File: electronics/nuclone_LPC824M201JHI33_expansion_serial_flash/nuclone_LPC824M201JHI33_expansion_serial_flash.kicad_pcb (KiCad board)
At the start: 2 copper layers, 45.8 x 25.5 mm, 23 parts, among them J1 nuclone_small_left, J2 nuclone_small_right, J3 DevBoardUartInput, J4 Conn_02x06_Odd_Even, U1 generic 25XNN serial flash

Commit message: LED place and route done, routing comleted
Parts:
- moved D2 12.7 mm to (75.6, 78.7)
- moved R10 12.7 mm to (73.0, 78.7)
- moved D1 12.7 mm to (75.6, 80.1)
- moved R9 12.7 mm to (73.0, 80.1)
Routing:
- net /VBUS: track 0.00 -> 29.4 mm
- net /LED1: track 0.00 -> 10.9 mm, vias 0 -> 1
- net /LED0: track 0.00 -> 8.07 mm, vias 0 -> 1
- net /VSS: track 2.45 -> 5.60 mm, vias 2 -> 3
- net Net-(D2-Pad2): track 0.00 -> 1.20 mm
- net Net-(D1-Pad2): track 0.00 -> 1.20 mm
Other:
- board text added: "Activity"
- board text added: "Blinky"
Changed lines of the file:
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@@
   (general
     (thickness 1.6)
-    (drawings 80)
-    (tracks 129)
+    (drawings 82)
+    (tracks 160)
     (zones 0)
     (modules 23)
@@
   )
   (module SquantorRcl:R_0402_hand (layer F.Cu)
-    (at 74.1 66 180)
+    (at 73 78.7 180)
     (descr "Resistor SMD 0402, reflow soldering, Vishay (see dcrcw.pdf)")
     (tags "resistor 0402")
@@
   )
   (module SquantorRcl:R_0402_hand (layer F.Cu)
-    (at 74.1 67.4 180)
+    (at 73 80.1 180)
     (descr "Resistor SMD 0402, reflow soldering, Vishay (see dcrcw.pdf)")
     (tags "resistor 0402")
@@
   )
   (module SquantorDiodes:LED_0603_hand (layer F.Cu)
-    (at 76.7 66 180)
+    (at 75.6 78.7 180)
     (descr "LED SMD 0603, reflow soldering, general purpose")
     (tags "LED 0603")
@@
   )
   (module SquantorDiodes:LED_0603_hand (layer F.Cu)
-    (at 76.7 67.4 180)
+    (at 75.6 80.1 180)
     (descr "LED SMD 0603, reflow soldering, general purpose")
     (tags "LED 0603")
@@
     (fp_line (start -0.5 -0.6) (end 0.5 -0.6) (layer B.SilkS) (width 0.15))
   )
+  (gr_text Blinky (at 75.7 77.2) (layer F.SilkS)
+    (effects (font (size 0.8 0.8) (thickness 0.12)))
+  )
+  (gr_text Activity (at 75.5 81.4) (layer F.SilkS)
+    (effects (font (size 0.8 0.8) (thickness 0.12)))
+  )
   (gr_text SIO3 (at 90 77.5) (layer F.SilkS)
     (effects (font (size 0.8 0.8) (thickness 0.12)))
@@
   (gr_line (start 63.1 99.1) (end 107.1 99.1) (layer Edge.Cuts) (width 0.15))
   (gr_line (start 62.2 74.5) (end 62.2 98.2) (layer Edge.Cuts) (width 0.15))
+  (segment (start 77 92.4) (end 77 94.1) (width 1) (layer F.Cu) (net 1))
+  (segment (start 77 94.1) (end 75.9 95.2) (width 1) (layer F.Cu) (net 1))
+  (segment (start 75.9 95.2) (end 69.9 95.2) (width 1) (layer F.Cu) (net 1))
+  (segment (start 69.9 95.2) (end 68.3 93.6) (width 1) (layer F.Cu) (net 1))
+  (segment (start 68.3 93.6) (end 68.3 78.4) (width 1) (layer F.Cu) (net 1))
+  (segment (start 67.37 77.47) (end 66.04 77.47) (width 1) (layer F.Cu) (net 1))
+  (segment (start 68.3 78.4) (end 67.37 77.47) (width 1) (layer F.Cu) (net 1))
   (via (at 87.5 84.1) (size 0.6) (drill 0.3) (layers F.Cu B.Cu) (net 8))
   (segment (start 87.505 84.105) (end 87.5 84.1) (width 0.4) (layer F.Cu) (net 8))
@@
   (via (at 82 84) (size 0.6) (drill 0.3) (layers F.Cu B.Cu) (net 8))
   (segment (start 82 83.2) (end 82 84) (width 0.4) (layer F.Cu) (net 8))
+  (via (at 77.5 79.4) (size 0.6) (drill 0.3) (layers F.Cu B.Cu) (net 8))
+  (segment (start 77.5 79.8) (end 77.5 79.4) (width 0.2) (layer F.Cu) (net 8))
+  (segment (start 77.2 80.1) (end 77.5 79.8) (width 0.2) (layer F.Cu) (net 8))
+  (segment (start 76.45 80.1) (end 77.2 80.1) (width 0.2) (layer F.Cu) (net 8))
+  (segment (start 77.5 79) (end 77.5 79.4) (width 0.2) (layer F.Cu) (net 8))
+  (segment (start 77.2 78.7) (end 77.5 79) (width 0.2) (layer F.Cu) (net 8))
+  (segment (start 76.45 78.7) (end 77.2 78.7) (width 0.2) (layer F.Cu) (net 8))
   (segment (start 63.5 74.93) (end 66.04 74.93) (width 1) (layer B.Cu) (net 9))
   (segment (start 104.14 74.93) (end 106.68 74.93) (width 1) (layer B.Cu) (net 9))
@@
   (segment (start 87.5 77.7) (end 87.5 77.15) (width 0.2) (layer F.Cu) (net 28))
   (segment (start 87.505 77.705) (end 87.5 77.7) (width 0.2) (layer F.Cu) (net 28))
+  (segment (start 74.75 80.1) (end 73.55 80.1) (width 0.2) (layer F.Cu) (net 29))
+  (segment (start 74.75 78.7) (end 73.55 78.7) (width 0.2) (layer F.Cu) (net 30))
+  (segment (start 66.04 82.55) (end 66.95 82.55) (width 0.2) (layer B.Cu) (net 35))
+  (via (at 69.3 82) (size 0.6) (drill 0.3) (layers F.Cu B.Cu) (net 35))
+  (segment (start 67.5 82) (end 69.3 82) (width 0.2) (layer B.Cu) (net 35))
+  (segment (start 66.95 82.55) (end 67.5 82) (width 0.2) (layer B.Cu) (net 35))
+  (segment (start 69.3 82) (end 69.7 82) (width 0.2) (layer F.Cu) (net 35))
+  (segment (start 69.7 82) (end 70 81.7) (width 0.2) (layer F.Cu) (net 35))
+  (segment (start 70 81.7) (end 70 80.6) (width 0.2) (layer F.Cu) (net 35))
+  (segment (start 70.5 80.1) (end 72.45 80.1) (width 0.2) (layer F.Cu) (net 35))
+  (segment (start 70 80.6) (end 70.5 80.1) (width 0.2) (layer F.Cu) (net 35))
+  (segment (start 63.5 82.55) (end 64.85 81.2) (width 0.2) (layer B.Cu) (net 36))
+  (via (at 69.3 81.2) (size 0.6) (drill 0.3) (layers F.Cu B.Cu) (net 36))
+  (segment (start 64.85 81.2) (end 69.3 81.2) (width 0.2) (layer B.Cu) (net 36))
+  (segment (start 69.3 80.6) (end 69.3 81.2) (width 0.2) (layer F.Cu) (net 36))
+  (segment (start 71.2 78.7) (end 69.3 80.6) (width 0.2) (layer F.Cu) (net 36))
+  (segment (start 72.45 78.7) (end 71.2 78.7) (width 0.2) (layer F.Cu) (net 36))
   (segment (start 102.59 80.01) (end 101.3 81.3) (width 0.2) (layer F.Cu) (net 41))
   (segment (start 94.62 81.3) (end 93.36 82.56) (width 0.2) (layer F.Cu) (net 41))

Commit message: fixed DRC error
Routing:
- net /VDD: track 71.0 -> 68.5 mm
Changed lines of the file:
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@@
     (thickness 1.6)
     (drawings 82)
-    (tracks 160)
+    (tracks 159)
     (zones 0)
     (modules 23)
@@
   (segment (start 76.45 78.7) (end 77.2 78.7) (width 0.2) (layer F.Cu) (net 8))
   (segment (start 63.5 74.93) (end 66.04 74.93) (width 1) (layer B.Cu) (net 9))
-  (segment (start 104.14 74.93) (end 106.68 74.93) (width 1) (layer B.Cu) (net 9))
   (segment (start 87.6 88.95) (end 88.45 88.95) (width 0.4) (layer F.Cu) (net 9))
   (segment (start 88.45 88.95) (end 88.9 88.5) (width 0.4) (layer F.Cu) (net 9))

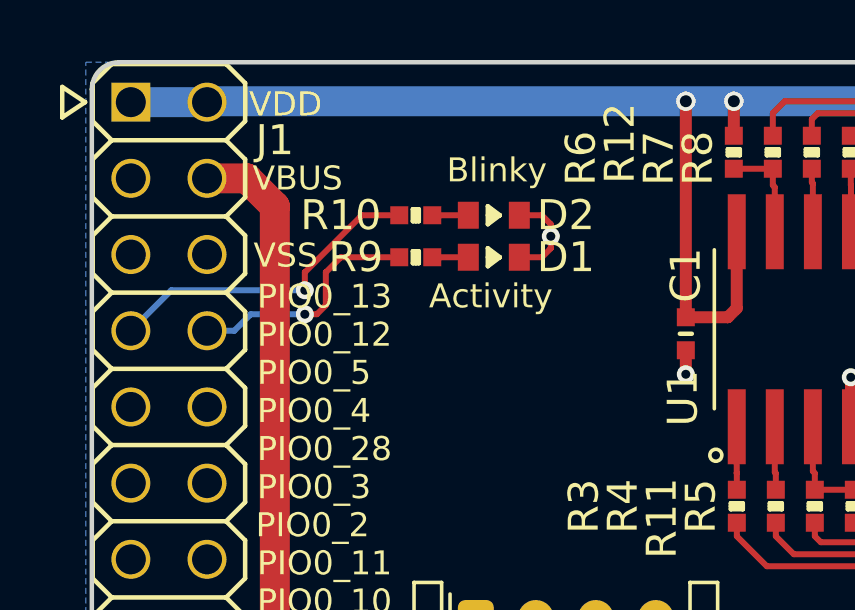
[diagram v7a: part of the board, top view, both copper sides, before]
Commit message: nicer LED placement
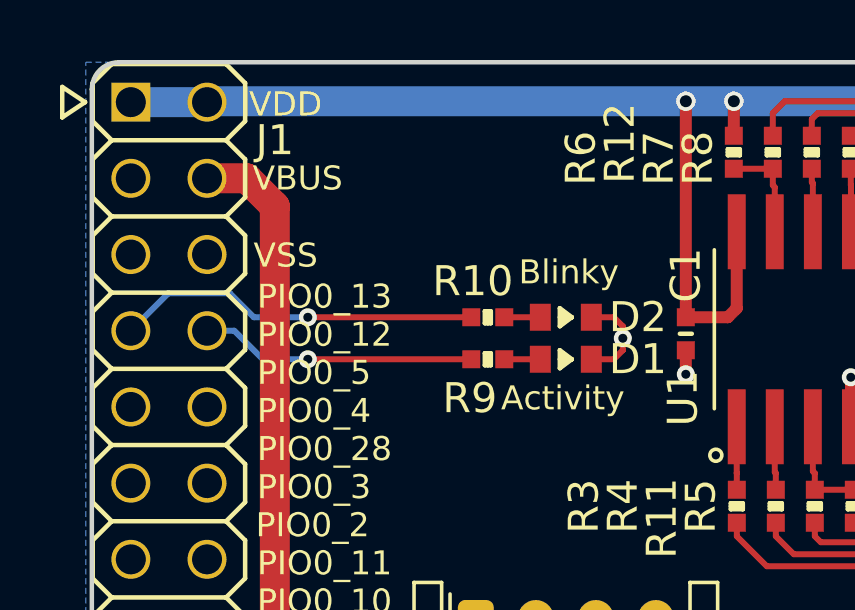
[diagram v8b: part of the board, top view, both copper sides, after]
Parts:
- moved D1 4.16 mm to (78.0, 83.5)
- moved R9 4.16 mm to (75.4, 83.5)
- moved D2 4.16 mm to (78.0, 82.1)
- moved R10 4.16 mm to (75.4, 82.1)
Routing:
- net /LED1: track 10.9 -> 12.2 mm
- net /LED0: track 8.07 -> 9.20 mm
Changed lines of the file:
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@@
     (thickness 1.6)
     (drawings 82)
-    (tracks 159)
+    (tracks 155)
     (zones 0)
     (modules 23)
@@
   )
   (module SquantorRcl:R_0402_hand (layer F.Cu)
-    (at 73 78.7 180)
+    (at 75.4 82.1 180)
     (descr "Resistor SMD 0402, reflow soldering, Vishay (see dcrcw.pdf)")
     (tags "resistor 0402")
     (attr smd)
-    (fp_text reference R10 (at 2.5 0) (layer F.SilkS)
-      (effects (font (size 1 1) (thickness 0.15)))
-    )
-    (fp_text value 4.7K (at 0 1.8) (layer F.Fab)
+    (fp_text reference R10 (at 0.5 1.2) (layer F.SilkS)
+      (effects (font (size 1 1) (thickness 0.15)))
+    )
+    (fp_text value 4.7K (at 0.7 1.2) (layer F.Fab)
       (effects (font (size 1 1) (thickness 0.15)))
     )
@@
   )
   (module SquantorRcl:R_0402_hand (layer F.Cu)
-    (at 73 80.1 180)
+    (at 75.4 83.5 180)
     (descr "Resistor SMD 0402, reflow soldering, Vishay (see dcrcw.pdf)")
     (tags "resistor 0402")
     (attr smd)
-    (fp_text reference R9 (at 2 0) (layer F.SilkS)
-      (effects (font (size 1 1) (thickness 0.15)))
-    )
-    (fp_text value 4.7K (at 0 1.8) (layer F.Fab)
+    (fp_text reference R9 (at 0.6 -1.3) (layer F.SilkS)
+      (effects (font (size 1 1) (thickness 0.15)))
+    )
+    (fp_text value 4.7K (at 0.7 -1.3) (layer F.Fab)
       (effects (font (size 1 1) (thickness 0.15)))
     )
@@
   )
   (module SquantorDiodes:LED_0603_hand (layer F.Cu)
-    (at 75.6 78.7 180)
+    (at 78 82.1 180)
     (descr "LED SMD 0603, reflow soldering, general purpose")
     (tags "LED 0603")
@@
   )
   (module SquantorDiodes:LED_0603_hand (layer F.Cu)
-    (at 75.6 80.1 180)
+    (at 78 83.5 180)
     (descr "LED SMD 0603, reflow soldering, general purpose")
     (tags "LED 0603")
@@
     (fp_line (start -0.5 -0.6) (end 0.5 -0.6) (layer B.SilkS) (width 0.15))
   )
-  (gr_text Blinky (at 75.7 77.2) (layer F.SilkS)
-    (effects (font (size 0.8 0.8) (thickness 0.12)))
-  )
-  (gr_text Activity (at 75.5 81.4) (layer F.SilkS)
+  (gr_text Blinky (at 78.1 80.6) (layer F.SilkS)
+    (effects (font (size 0.8 0.8) (thickness 0.12)))
+  )
+  (gr_text Activity (at 77.9 84.8) (layer F.SilkS)
     (effects (font (size 0.8 0.8) (thickness 0.12)))
   )
@@
   (via (at 82 84) (size 0.6) (drill 0.3) (layers F.Cu B.Cu) (net 8))
   (segment (start 82 83.2) (end 82 84) (width 0.4) (layer F.Cu) (net 8))
-  (via (at 77.5 79.4) (size 0.6) (drill 0.3) (layers F.Cu B.Cu) (net 8))
-  (segment (start 77.5 79.8) (end 77.5 79.4) (width 0.2) (layer F.Cu) (net 8))
-  (segment (start 77.2 80.1) (end 77.5 79.8) (width 0.2) (layer F.Cu) (net 8))
-  (segment (start 76.45 80.1) (end 77.2 80.1) (width 0.2) (layer F.Cu) (net 8))
-  (segment (start 77.5 79) (end 77.5 79.4) (width 0.2) (layer F.Cu) (net 8))
-  (segment (start 77.2 78.7) (end 77.5 79) (width 0.2) (layer F.Cu) (net 8))
-  (segment (start 76.45 78.7) (end 77.2 78.7) (width 0.2) (layer F.Cu) (net 8))
+  (via (at 79.9 82.8) (size 0.6) (drill 0.3) (layers F.Cu B.Cu) (net 8))
+  (segment (start 79.9 83.2) (end 79.9 82.8) (width 0.2) (layer F.Cu) (net 8))
+  (segment (start 79.6 83.5) (end 79.9 83.2) (width 0.2) (layer F.Cu) (net 8))
+  (segment (start 78.85 83.5) (end 79.6 83.5) (width 0.2) (layer F.Cu) (net 8))
+  (segment (start 79.9 82.4) (end 79.9 82.8) (width 0.2) (layer F.Cu) (net 8))
+  (segment (start 79.6 82.1) (end 79.9 82.4) (width 0.2) (layer F.Cu) (net 8))
+  (segment (start 78.85 82.1) (end 79.6 82.1) (width 0.2) (layer F.Cu) (net 8))
   (segment (start 63.5 74.93) (end 66.04 74.93) (width 1) (layer B.Cu) (net 9))
   (segment (start 87.6 88.95) (end 88.45 88.95) (width 0.4) (layer F.Cu) (net 9))
@@
   (segment (start 87.5 77.7) (end 87.5 77.15) (width 0.2) (layer F.Cu) (net 28))
   (segment (start 87.505 77.705) (end 87.5 77.7) (width 0.2) (layer F.Cu) (net 28))
-  (segment (start 74.75 80.1) (end 73.55 80.1) (width 0.2) (layer F.Cu) (net 29))
-  (segment (start 74.75 78.7) (end 73.55 78.7) (width 0.2) (layer F.Cu) (net 30))
-  (segment (start 66.04 82.55) (end 66.95 82.55) (width 0.2) (layer B.Cu) (net 35))
-  (via (at 69.3 82) (size 0.6) (drill 0.3) (layers F.Cu B.Cu) (net 35))
-  (segment (start 67.5 82) (end 69.3 82) (width 0.2) (layer B.Cu) (net 35))
-  (segment (start 66.95 82.55) (end 67.5 82) (width 0.2) (layer B.Cu) (net 35))
-  (segment (start 69.3 82) (end 69.7 82) (width 0.2) (layer F.Cu) (net 35))
-  (segment (start 69.7 82) (end 70 81.7) (width 0.2) (layer F.Cu) (net 35))
-  (segment (start 70 81.7) (end 70 80.6) (width 0.2) (layer F.Cu) (net 35))
-  (segment (start 70.5 80.1) (end 72.45 80.1) (width 0.2) (layer F.Cu) (net 35))
-  (segment (start 70 80.6) (end 70.5 80.1) (width 0.2) (layer F.Cu) (net 35))
-  (segment (start 63.5 82.55) (end 64.85 81.2) (width 0.2) (layer B.Cu) (net 36))
-  (via (at 69.3 81.2) (size 0.6) (drill 0.3) (layers F.Cu B.Cu) (net 36))
-  (segment (start 64.85 81.2) (end 69.3 81.2) (width 0.2) (layer B.Cu) (net 36))
-  (segment (start 69.3 80.6) (end 69.3 81.2) (width 0.2) (layer F.Cu) (net 36))
-  (segment (start 71.2 78.7) (end 69.3 80.6) (width 0.2) (layer F.Cu) (net 36))
-  (segment (start 72.45 78.7) (end 71.2 78.7) (width 0.2) (layer F.Cu) (net 36))
+  (segment (start 77.15 83.5) (end 75.95 83.5) (width 0.2) (layer F.Cu) (net 29))
+  (segment (start 77.15 82.1) (end 75.95 82.1) (width 0.2) (layer F.Cu) (net 30))
+  (segment (start 66.95 82.55) (end 66.04 82.55) (width 0.2) (layer B.Cu) (net 35))
+  (segment (start 67.9 83.5) (end 66.95 82.55) (width 0.2) (layer B.Cu) (net 35))
+  (segment (start 69.4 83.5) (end 67.9 83.5) (width 0.2) (layer B.Cu) (net 35))
+  (via (at 69.4 83.5) (size 0.6) (drill 0.3) (layers F.Cu B.Cu) (net 35))
+  (segment (start 74.85 83.5) (end 69.4 83.5) (width 0.2) (layer F.Cu) (net 35))
+  (via (at 69.4 82.1) (size 0.6) (drill 0.3) (layers F.Cu B.Cu) (net 36))
+  (segment (start 64.75 81.3) (end 63.5 82.55) (width 0.2) (layer B.Cu) (net 36))
+  (segment (start 66.8 81.3) (end 64.75 81.3) (width 0.2) (layer B.Cu) (net 36))
+  (segment (start 67.6 82.1) (end 66.8 81.3) (width 0.2) (layer B.Cu) (net 36))
+  (segment (start 69.4 82.1) (end 67.6 82.1) (width 0.2) (layer B.Cu) (net 36))
+  (segment (start 74.85 82.1) (end 69.4 82.1) (width 0.2) (layer F.Cu) (net 36))
   (segment (start 102.59 80.01) (end 101.3 81.3) (width 0.2) (layer F.Cu) (net 41))
   (segment (start 94.62 81.3) (end 93.36 82.56) (width 0.2) (layer F.Cu) (net 41))
